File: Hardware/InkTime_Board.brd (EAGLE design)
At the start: 46 x 35 mm, 105 parts, among them IC1 RT6160AWSC, IC2 BMA423, IC3 BQ25180YBGR, IC4 DRV2605YZFR, J1 TC2030-IDC, J2 503480-2400, J4 KH-TYPE-C-16P_KH-TYPE-C-16P, Q1 20V/4.2A/52mΩ/1.4W, Q3 SI1308EDL-T1-GE3, U1 MAX17048G+T10, X1 32MHZ, X2 32.768KHZ

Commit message: Rerouted some signals
Signed-off-by: Andrei Rusanescu <andreirusanescu154@gmail.com>
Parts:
- moved TP_ON 19.7 mm to (23.2, 8.62)
- moved U1 10.6 mm to (35.8, -6.56)
- moved C27 9.57 mm to (39.7, -3.58)
- moved C39 3.90 mm to (36.5, -9.81)
- moved C15 2.24 mm to (47.6, 0.37)
- moved C38 1.97 mm to (38.4, -9.88)
- moved C10 1.80 mm to (53.8, -3.66)
- moved C14 1.71 mm to (44.7, 1.27)
- moved L2 1.60 mm to (47.1, 4.94)
- moved L3 1.57 mm to (50.1, 4.96)
- moved C24 1.50 mm to (40.6, -13.4)
- moved C1 1.37 mm to (52.7, -2.01)
- moved NRF52840_QF 1.36 mm to (48.6, -4.69)
- moved C13 1.35 mm to (49.9, -0.58)
- moved C16 1.34 mm to (49.1, -0.57)
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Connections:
- removed net 3V3/1.7D: C34.1, IC4.C2, Q1.2, R_PWR_EPD.2
- removed net 3V3/2.4A: C12.1, C14.1, C19.1, C7.1, C8.1, IC2.10, IC2.3, IC2.7, J1.1, NRF52840_QF.P$A22, NRF52840_QF.P$AD14, NRF52840_QF.P$AD23, NRF52840_QF.P$B1, TP_3.3V.TP, TP_3V3.TP
- removed net ALERT/1.6C: U1.5
- removed net ALERT/2.5C: NRF52840_QF.P$J24
- removed net D+/1.5D: D3.4
- removed net D+/2.7D: NRF52840_QF.P$AD6
- removed net D-/1.5D: D3.6
- removed net D-/2.7D: NRF52840_QF.P$AD4
- removed net EPD_BUSY/1.5D: J2.9
- removed net EPD_BUSY/2.2D: NRF52840_QF.P$AD12
- removed net EPD_CS/1.4C: J2.12
- removed net EPD_CS/2.2D: NRF52840_QF.P$K2
- removed net EPD_DC/1.5D: J2.11
- removed net EPD_DC/2.2D: NRF52840_QF.P$AD10
- removed net EPD_RST/1.5D: J2.10
- removed net EPD_RST/2.2D: NRF52840_QF.P$AC11
- removed net HAPTIC_EN/1.4C: IC4.A1
- removed net HAPTIC_EN/2.6A: NRF52840_QF.P$T2
- removed net MOSI/1.5B: J2.14
- removed net MOSI/2.2D: NRF52840_QF.P$B13
- removed net P0.13/1.5D: C30.1, R7.1, SW_UP.2
- removed net P0.13/2.6C: NRF52840_QF.P$AD8
- removed net P0.14/1.5D: C31.1, R8.1, SW_ENT.2
- removed net P0.14/2.7C: NRF52840_QF.P$AC9
- removed net P1.01/1.6C: Q1.1, R_PWR_EPD.1
- removed net P1.01/2.4B: NRF52840_QF.P$Y23
- removed net P1.02/1.6C: C29.1, R9.1, SW_DN.2
- removed net P1.02/2.8C: NRF52840_QF.P$W24
- removed net SCK/1.5B: J2.13
- removed net SCK/2.2D: NRF52840_QF.P$A12
- removed net SCL/1.4C: IC4.C1, U1.7
- removed net SCL/2.4C: IC2.12, IC3.B1, NRF52840_QF.P$M2, R1.1, R3.2, TP3.TP
- removed net SDA/1.4C: IC4.B2, U1.8
- removed net SDA/2.4C: IC2.2, IC3.C1, NRF52840_QF.P$L1, R2.1, R4.2, TP4.TP
- removed net VBAT/1.2A: C27.1, U1.2, U1.3
- removed net VBAT/2.5C: C37.1, IC3.C2
- removed net VBUS/1.5D: C42.1, C43.1, D3.5, J4.A4_B9, J4.A9_B4
- removed net VBUS/2.6D: C21.1, C38.1, IC3.A2, NRF52840_QF.P$AD2
- new net 3V3: C12.1, C14.1, C19.1, C34.1, C7.1, C8.1, IC2.10, IC2.3, IC2.7, IC4.C2, J1.1, NRF52840_QF.P$A22, NRF52840_QF.P$AD14, NRF52840_QF.P$AD23, NRF52840_QF.P$B1, Q1.2, R_PWR_EPD.2, TP_3.3V.TP, TP_3V3.TP
- new net ALERT: NRF52840_QF.P$J24, U1.5
- new net D+: D3.4, NRF52840_QF.P$AD6
- new net D-: D3.6, NRF52840_QF.P$AD4
- new net EPD_BUSY: J2.9, NRF52840_QF.P$AD12
- new net EPD_CS: J2.12, NRF52840_QF.P$K2
- new net EPD_DC: J2.11, NRF52840_QF.P$AD10
- new net EPD_RST: J2.10, NRF52840_QF.P$AD18
- new net HAPTIC_EN: IC4.A1, NRF52840_QF.P$U1
- new net MOSI: J2.14, NRF52840_QF.P$B13
- new net P0.13: C30.1, NRF52840_QF.P$AD8, R7.1, SW_UP.2
- new net P0.14: C31.1, NRF52840_QF.P$AD16, R8.1, SW_ENT.2
- new net P1.01: NRF52840_QF.P$Y23, Q1.1, R_PWR_EPD.1
- new net P1.02: C29.1, NRF52840_QF.P$W24, R9.1, SW_DN.2
- new net SCK: J2.13, NRF52840_QF.P$A12
- new net SCL: IC2.12, IC3.B1, IC4.C1, NRF52840_QF.P$M2, R1.1, R3.2, TP3.TP, U1.7
- new net SDA: IC2.2, IC3.C1, IC4.B2, NRF52840_QF.P$L1, R2.1, R4.2, TP4.TP, U1.8
- new net VBAT: C27.1, C37.1, IC3.C2, U1.2, U1.3
- new net VBUS: C21.1, C38.1, C42.1, C43.1, D3.5, IC3.A2, J4.A4_B9, J4.A9_B4, NRF52840_QF.P$AD2
- net IMU_INT2: now also NRF52840_QF.P$P2; no longer NRF52840_QF.P$R1
- net P0.20: now also NRF52840_QF.P$AC9; no longer NRF52840_QF.P$AD16
- net P0.22: now also NRF52840_QF.P$AC11; no longer NRF52840_QF.P$AD18
- net P0.24: now also NRF52840_QF.P$AD20; no longer NRF52840_QF.P$AC13
- net P1.09: now also NRF52840_QF.P$R1; no longer NRF52840_QF.P$P2
- net PMIC_INT: now also NRF52840_QF.P$T2; no longer NRF52840_QF.P$U1
- net RESET: now also NRF52840_QF.P$AC13; no longer NRF52840_QF.P$AD20
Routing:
- net 3V3: track 0.00 -> 86.8 mm, vias 0 -> 9
- net 3V3/2.4A: track 70.8 -> 0.00 mm, vias 12 -> 0
- net SCL: track 0.00 -> 59.4 mm, vias 0 -> 6
- net GND: track 619.5 -> 560.7 mm, vias 57 -> 70
- net VBUS: track 0.00 -> 56.8 mm, vias 0 -> 4
- net SDA: track 0.00 -> 53.8 mm, vias 0 -> 7
- net EPD_DC: track 0.00 -> 42.7 mm, vias 0 -> 2
- net SCL/2.4C: track 37.2 -> 0.00 mm, vias 4 -> 0
- net EPD_BUSY: track 0.00 -> 36.2 mm, vias 0 -> 3
- net EPD_RST: track 0.00 -> 31.1 mm, vias 0 -> 2
- net HAPTIC_EN: track 0.00 -> 28.1 mm, vias 0 -> 2
- net P0.13: track 0.00 -> 26.7 mm, vias 0 -> 2
- net P1.01: track 0.00 -> 25.9 mm, vias 0 -> 2
- net MOSI: track 0.00 -> 24.9 mm, vias 0 -> 2
- net D+: track 0.00 -> 24.3 mm, vias 0 -> 2
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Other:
- board text added: "3V3"
- board text added: "SCL"
- board text added: "SDA"
- board text removed: "3V3/2.4A"
- board text removed: "SCL/2.4C"
- board text removed: "SDA/2.4C"

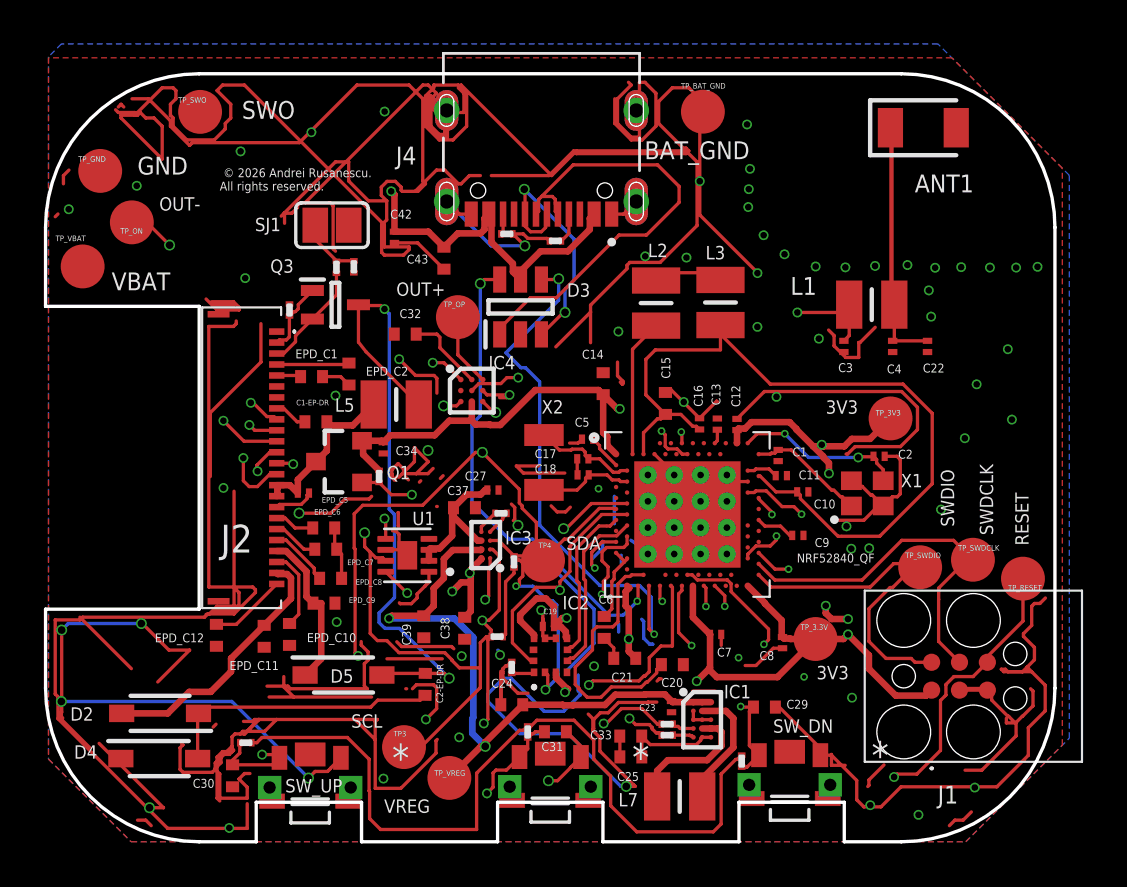
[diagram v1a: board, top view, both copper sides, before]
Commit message: Rerouted some other signals. Minor changes to README.md
Signed-off-by: Andrei Rusanescu <andreirusanescu154@gmail.com>
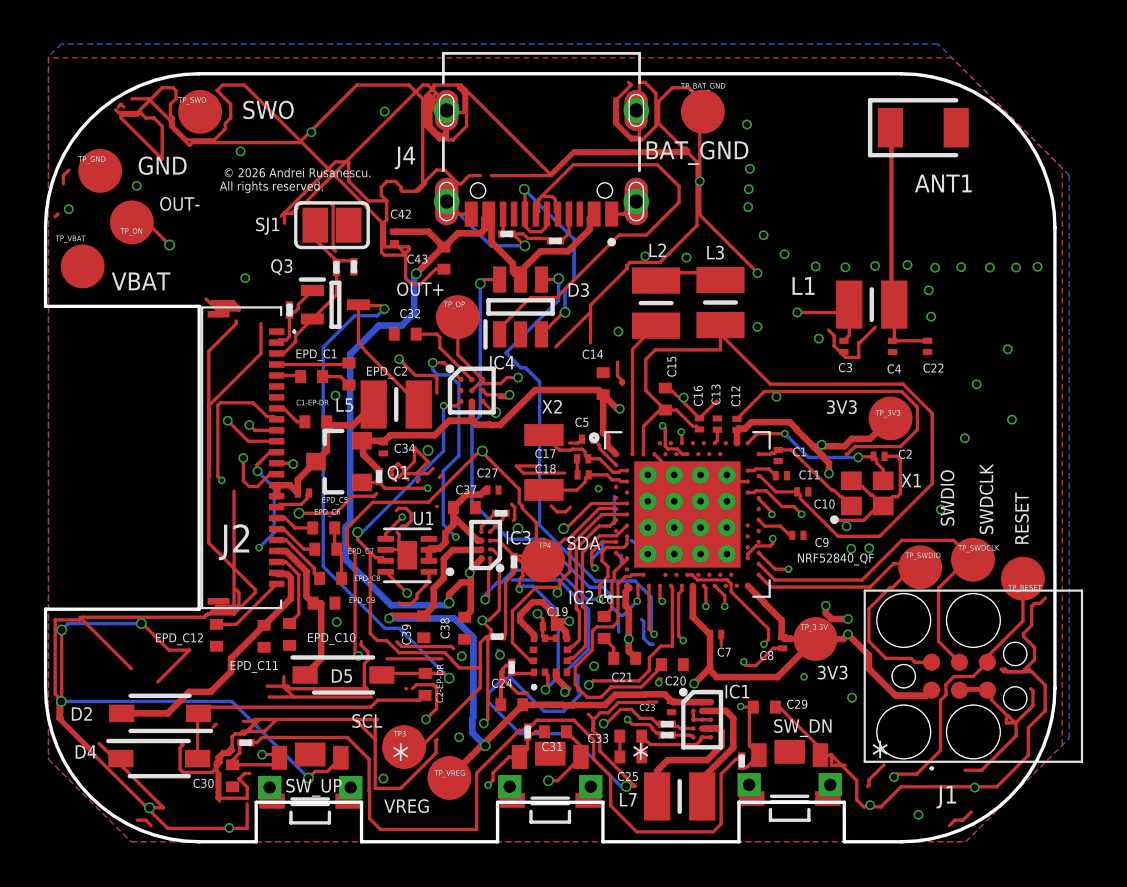
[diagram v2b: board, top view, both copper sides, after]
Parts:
- moved C15 0.20 mm to (47.6, 0.56)
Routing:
- net HAPTIC_EN: track 28.1 -> 21.9 mm, vias 2 -> 3
- net P0.13: track 26.7 -> 32.8 mm
- net VBUS: track 56.8 -> 53.6 mm
- net N$28: track 29.2 -> 31.5 mm
- net P1.01: track 25.9 -> 23.7 mm
- net EPD_DC: track 42.7 -> 44.7 mm
- net EPD_RST: track 31.1 -> 32.2 mm
- net P0.14: track 20.9 -> 21.8 mm
- net GND: track 560.7 -> 561.5 mm, vias 70 -> 71
- net EPD_BUSY: track 36.2 -> 35.8 mm, vias 3 -> 2
- net EPD_CS: track 23.8 -> 23.5 mm, vias 2 -> 3

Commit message: Rerouted some more. Added BGA
Signed-off-by: Andrei Rusanescu <andreirusanescu154@gmail.com>
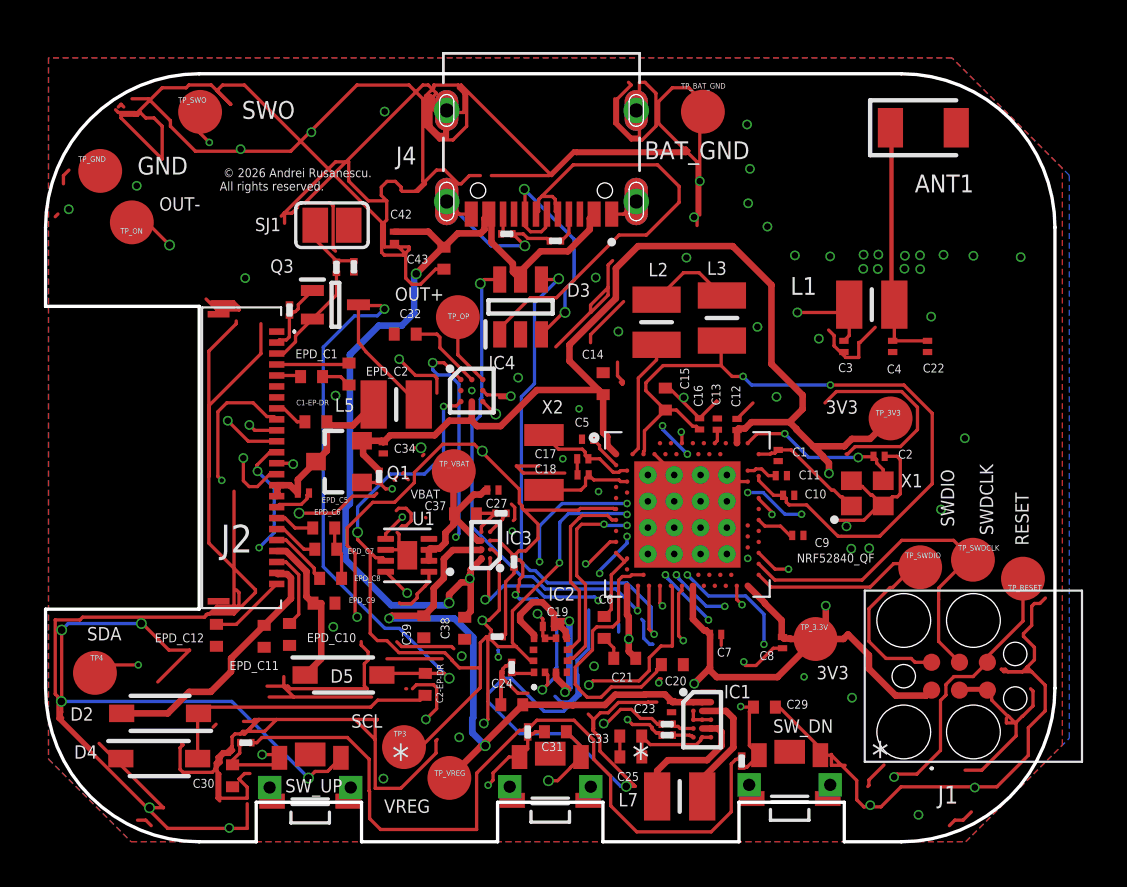
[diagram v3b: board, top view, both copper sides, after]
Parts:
- moved TP4 21.1 mm to (21.6, -11.9)
- moved TP_VBAT 19.3 mm to (37.9, -2.72)
- moved L2 0.87 mm to (47.2, 4.07)
- moved L3 0.71 mm to (50.1, 4.26)
- moved C10 0.66 mm to (53.2, -3.82)
- moved C37 0.29 mm to (38.4, -4.67)
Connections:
- removed net N$33: TP_VBAT.TP
- removed net SWO\: NRF52840_QF.P$AD22
- net EPD_RST: now also NRF52840_QF.P$AC11; no longer NRF52840_QF.P$AD18
- net P0.14: now also NRF52840_QF.P$AC9; no longer NRF52840_QF.P$AD16
- net P0.20: now also NRF52840_QF.P$AD16; no longer NRF52840_QF.P$AC9
- net P0.22: now also NRF52840_QF.P$AD18; no longer NRF52840_QF.P$AC11
- net SWO: now also NRF52840_QF.P$AD22
- net VBAT: now also TP_VBAT.TP
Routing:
- net SWO: track 0.00 -> 44.4 mm, vias 0 -> 2
- net GND: track 561.5 -> 534.2 mm
- net SDA: track 53.8 -> 65.0 mm, vias 7 -> 9
- net 3V3: track 86.3 -> 97.5 mm, vias 9 -> 5
- net ALERT: track 22.5 -> 25.6 mm
- net P1.01: track 23.7 -> 20.8 mm
- net HAPTIC_EN: track 21.9 -> 19.3 mm
- net SCL: track 59.8 -> 57.9 mm, vias 6 -> 7
- net EPD_DC: track 44.7 -> 42.8 mm
- net VBAT: track 6.95 -> 8.52 mm
- net PMIC_INT: track 12.5 -> 11.1 mm, vias 2 -> 4
- net EPD_CS: track 23.5 -> 24.8 mm, vias 3 -> 4
- net P0.14: track 21.8 -> 23.0 mm, vias 2 -> 3
- net EPD_BUSY: track 35.8 -> 34.6 mm
- net IMU_INT1: track 7.30 -> 8.43 mm
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
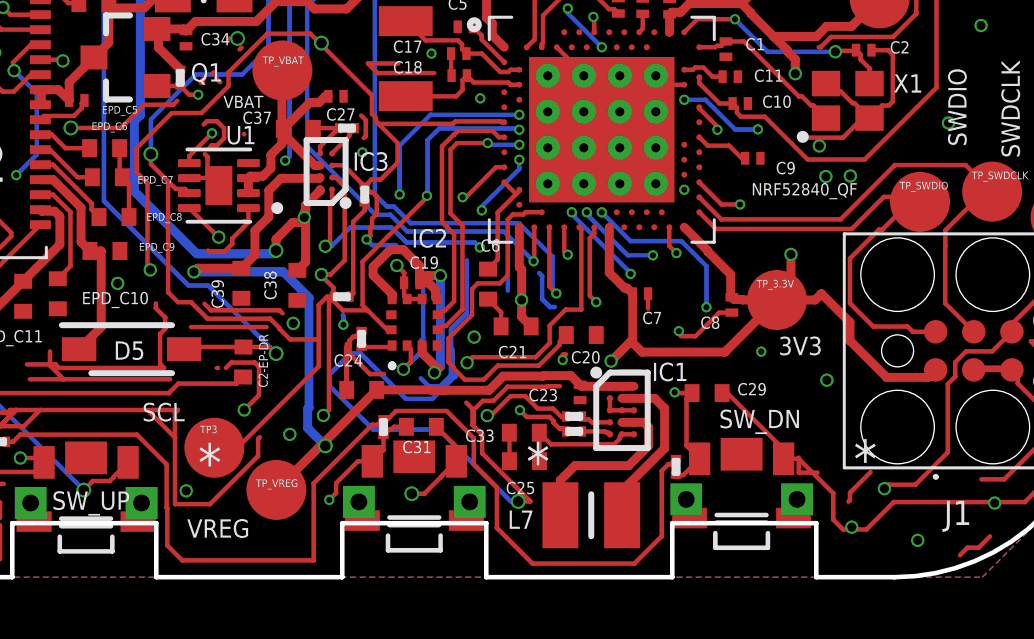
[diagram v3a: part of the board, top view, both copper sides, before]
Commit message: Upated routing. Fixes #2, fixes #3, fixes #4, and resolves #5
Signed-off-by: Andrei Rusanescu <andreirusanescu154@gmail.com>
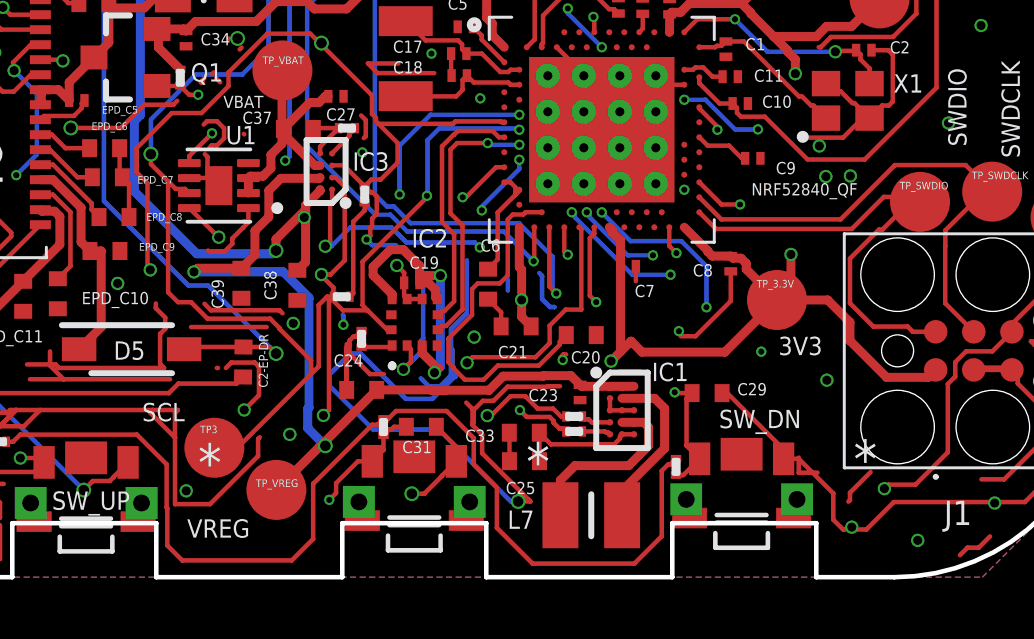
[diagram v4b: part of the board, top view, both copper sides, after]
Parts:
- moved C8 1.37 mm to (52.9, -9.16)
- moved C7 1.00 mm to (49.4, -9.25)
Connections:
- removed net N$8: TP_GND.TP
- net GND: now also TP_GND.TP
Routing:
- net P0.14: track 23.0 -> 24.5 mm
- net GND: track 534.2 -> 535.3 mm
- net VBUS: track 53.2 -> 53.8 mm
